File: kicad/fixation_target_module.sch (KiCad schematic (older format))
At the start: 3 parts

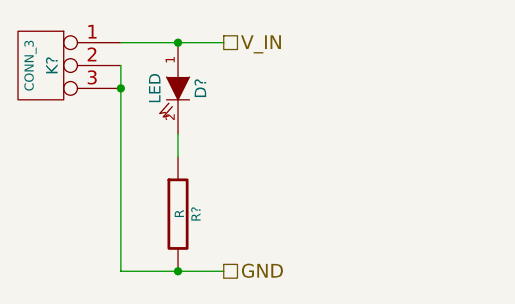
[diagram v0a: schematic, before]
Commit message: finished board v1.0
sent to freedfm for check
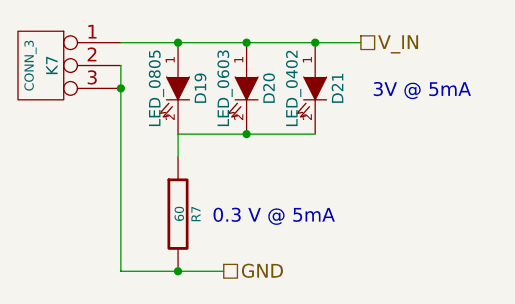
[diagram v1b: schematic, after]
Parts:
- added D2: LED_0603, ~, symbol LED
- added D3: LED_0402, ~, symbol LED
- D1: renamed from D?; value LED -> LED_0805
- R1: renamed from R?; value R -> 60
- gave numbers to parts that had none: 1
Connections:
- net V_IN: now also D2.1 (A), D3.1 (A)
- net at D1.2 (K), R1.1: now also D2.2 (K), D3.2 (K)
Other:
- note added: "0.3 V @ 5mA"
- note added: "3V @ 5mA"
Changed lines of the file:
@@
 LIBS:contrib
 LIBS:valves
+LIBS:chroma_spotlight
 LIBS:spiky_sphere-cache
 EELAYER 27 0
@@
 $EndDescr
 $Comp
-L R R?
+L R R1
 U 1 1 52F1A596
 P 8400 3550
-AR Path="/52F1AAB5/52F1A596" Ref="R?"  Part="1"
-AR Path="/52F1B071/52F1A596" Ref="R?"  Part="1"
-AR Path="/52F1B075/52F1A596" Ref="R?"  Part="1"
-AR Path="/52F1D479/52F1A596" Ref="R?"  Part="1"
-AR Path="/52F1D47D/52F1A596" Ref="R?"  Part="1"
-AR Path="/52F1D481/52F1A596" Ref="R?"  Part="1"
-AR Path="/52F1D485/52F1A596" Ref="R?"  Part="1"
-F 0 "R?" V 8480 3550 40  0000 C CNN
-F 1 "R" V 8407 3551 40  0000 C CNN
+AR Path="/52F1AAB5/52F1A596" Ref="R1"  Part="1"
+AR Path="/52F1B071/52F1A596" Ref="R2"  Part="1"
+AR Path="/52F1B075/52F1A596" Ref="R3"  Part="1"
+AR Path="/52F1D479/52F1A596" Ref="R4"  Part="1"
+AR Path="/52F1D47D/52F1A596" Ref="R5"  Part="1"
+AR Path="/52F1D481/52F1A596" Ref="R6"  Part="1"
+AR Path="/52F1D485/52F1A596" Ref="R7"  Part="1"
+F 0 "R7" V 8480 3550 40  0000 C CNN
+F 1 "60" V 8407 3551 40  0000 C CNN
 F 2 "~" V 8330 3550 30  0000 C CNN
 F 3 "~" H 8400 3550 30  0000 C CNN
@@
 $EndComp
 $Comp
-L CONN_3 K?
+L CONN_3 K1
 U 1 1 52F1A5A5
 P 7800 2900
-AR Path="/52F1AAB5/52F1A5A5" Ref="K?"  Part="1"
-AR Path="/52F1B071/52F1A5A5" Ref="K?"  Part="1"
-AR Path="/52F1B075/52F1A5A5" Ref="K?"  Part="1"
-AR Path="/52F1D479/52F1A5A5" Ref="K?"  Part="1"
-AR Path="/52F1D47D/52F1A5A5" Ref="K?"  Part="1"
-AR Path="/52F1D481/52F1A5A5" Ref="K?"  Part="1"
-AR Path="/52F1D485/52F1A5A5" Ref="K?"  Part="1"
-F 0 "K?" V 7750 2900 50  0000 C CNN
+AR Path="/52F1AAB5/52F1A5A5" Ref="K1"  Part="1"
+AR Path="/52F1B071/52F1A5A5" Ref="K2"  Part="1"
+AR Path="/52F1B075/52F1A5A5" Ref="K3"  Part="1"
+AR Path="/52F1D479/52F1A5A5" Ref="K4"  Part="1"
+AR Path="/52F1D47D/52F1A5A5" Ref="K5"  Part="1"
+AR Path="/52F1D481/52F1A5A5" Ref="K6"  Part="1"
+AR Path="/52F1D485/52F1A5A5" Ref="K7"  Part="1"
+F 0 "K7" V 7750 2900 50  0000 C CNN
 F 1 "CONN_3" V 7850 2900 40  0000 C CNN
 F 2 "~" H 7800 2900 60  0000 C CNN
@@
 $EndComp
 $Comp
-L LED D?
+L LED D1
 U 1 1 52F1A5B4
 P 8400 3000
-AR Path="/52F1AAB5/52F1A5B4" Ref="D?"  Part="1"
-AR Path="/52F1B071/52F1A5B4" Ref="D?"  Part="1"
-AR Path="/52F1B075/52F1A5B4" Ref="D?"  Part="1"
-AR Path="/52F1D479/52F1A5B4" Ref="D?"  Part="1"
-AR Path="/52F1D47D/52F1A5B4" Ref="D?"  Part="1"
-AR Path="/52F1D481/52F1A5B4" Ref="D?"  Part="1"
-AR Path="/52F1D485/52F1A5B4" Ref="D?"  Part="1"
-F 0 "D?" H 8400 3100 50  0000 C CNN
-F 1 "LED" H 8400 2900 50  0000 C CNN
+AR Path="/52F1AAB5/52F1A5B4" Ref="D1"  Part="1"
+AR Path="/52F1B071/52F1A5B4" Ref="D4"  Part="1"
+AR Path="/52F1B075/52F1A5B4" Ref="D7"  Part="1"
+AR Path="/52F1D479/52F1A5B4" Ref="D10"  Part="1"
+AR Path="/52F1D47D/52F1A5B4" Ref="D13"  Part="1"
+AR Path="/52F1D481/52F1A5B4" Ref="D16"  Part="1"
+AR Path="/52F1D485/52F1A5B4" Ref="D19"  Part="1"
+F 0 "D19" H 8400 3100 50  0000 C CNN
+F 1 "LED_0805" H 8400 2900 50  0000 C CNN
 F 2 "~" H 8400 3000 60  0000 C CNN
 F 3 "~" H 8400 3000 60  0000 C CNN
@@
 Connection ~ 8150 3000
 Wire Wire Line
-	8150 2800 8600 2800
+	8150 2800 9200 2800
 Connection ~ 8400 2800
 Connection ~ 8400 3800
-Text HLabel 8600 2800 2    60   UnSpc ~ 0
+Text HLabel 9200 2800 2    60   UnSpc ~ 0
 V_IN
 Text HLabel 8600 3800 2    60   UnSpc ~ 0
 GND
+$Comp
+L LED D2
+U 1 1 52F28B77
+P 8700 3000
+AR Path="/52F1AAB5/52F28B77" Ref="D2"  Part="1"
+AR Path="/52F1B071/52F28B77" Ref="D5"  Part="1"
+AR Path="/52F1B075/52F28B77" Ref="D8"  Part="1"
+AR Path="/52F1D479/52F28B77" Ref="D11"  Part="1"
+AR Path="/52F1D47D/52F28B77" Ref="D14"  Part="1"
+AR Path="/52F1D481/52F28B77" Ref="D17"  Part="1"
+AR Path="/52F1D485/52F28B77" Ref="D20"  Part="1"
+F 0 "D20" H 8700 3100 50  0000 C CNN
+F 1 "LED_0603" H 8700 2900 50  0000 C CNN
+F 2 "~" H 8700 3000 60  0000 C CNN
+F 3 "~" H 8700 3000 60  0000 C CNN
+	1    8700 3000
+	0    1    1    0
+$EndComp
+$Comp
+L LED D3
+U 1 1 52F28B7D
+P 9000 3000
+AR Path="/52F1AAB5/52F28B7D" Ref="D3"  Part="1"
+AR Path="/52F1B071/52F28B7D" Ref="D6"  Part="1"
+AR Path="/52F1B075/52F28B7D" Ref="D9"  Part="1"
+AR Path="/52F1D479/52F28B7D" Ref="D12"  Part="1"
+AR Path="/52F1D47D/52F28B7D" Ref="D15"  Part="1"
+AR Path="/52F1D481/52F28B7D" Ref="D18"  Part="1"
+AR Path="/52F1D485/52F28B7D" Ref="D21"  Part="1"
+F 0 "D21" H 9000 3100 50  0000 C CNN
+F 1 "LED_0402" H 9000 2900 50  0000 C CNN
+F 2 "~" H 9000 3000 60  0000 C CNN
+F 3 "~" H 9000 3000 60  0000 C CNN
+	1    9000 3000
+	0    1    1    0
+$EndComp
+Wire Wire Line
+	8400 3200 9000 3200
+Connection ~ 8700 3200
+Connection ~ 8700 2800
+Connection ~ 9000 2800
+Text Notes 8550 3600 0    60   ~ 0
+0.3 V @ 5mA
+Text Notes 9250 3050 0    60   ~ 0
+3V @ 5mA
 $EndSCHEMATC

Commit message: small changes and added illum boards
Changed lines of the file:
@@
 $Descr A4 11693 8268
 encoding utf-8
-Sheet 2 8
+Sheet 8 8
 Title ""
-Date "5 feb 2014"
+Date "6 feb 2014"
 Rev ""
 Comp ""
@@
 AR Path="/52F1D481/52F1A596" Ref="R6"  Part="1"
 AR Path="/52F1D485/52F1A596" Ref="R7"  Part="1"
-F 0 "R7" V 8480 3550 40  0000 C CNN
+F 0 "R6" V 8480 3550 40  0000 C CNN
 F 1 "60" V 8407 3551 40  0000 C CNN
 F 2 "~" V 8330 3550 30  0000 C CNN
@@
 AR Path="/52F1D481/52F1A5A5" Ref="K6"  Part="1"
 AR Path="/52F1D485/52F1A5A5" Ref="K7"  Part="1"
-F 0 "K7" V 7750 2900 50  0000 C CNN
+F 0 "K6" V 7750 2900 50  0000 C CNN
 F 1 "CONN_3" V 7850 2900 40  0000 C CNN
 F 2 "~" H 7800 2900 60  0000 C CNN
@@
 AR Path="/52F1D481/52F1A5B4" Ref="D16"  Part="1"
 AR Path="/52F1D485/52F1A5B4" Ref="D19"  Part="1"
-F 0 "D19" H 8400 3100 50  0000 C CNN
+F 0 "D16" H 8400 3100 50  0000 C CNN
 F 1 "LED_0805" H 8400 2900 50  0000 C CNN
 F 2 "~" H 8400 3000 60  0000 C CNN
@@
 AR Path="/52F1D481/52F28B77" Ref="D17"  Part="1"
 AR Path="/52F1D485/52F28B77" Ref="D20"  Part="1"
-F 0 "D20" H 8700 3100 50  0000 C CNN
+F 0 "D17" H 8700 3100 50  0000 C CNN
 F 1 "LED_0603" H 8700 2900 50  0000 C CNN
 F 2 "~" H 8700 3000 60  0000 C CNN
@@
 AR Path="/52F1D481/52F28B7D" Ref="D18"  Part="1"
 AR Path="/52F1D485/52F28B7D" Ref="D21"  Part="1"
-F 0 "D21" H 9000 3100 50  0000 C CNN
+F 0 "D18" H 9000 3100 50  0000 C CNN
 F 1 "LED_0402" H 9000 2900 50  0000 C CNN
 F 2 "~" H 9000 3000 60  0000 C CNN
